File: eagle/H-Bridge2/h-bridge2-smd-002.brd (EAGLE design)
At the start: 100 x 80 mm, 38 parts

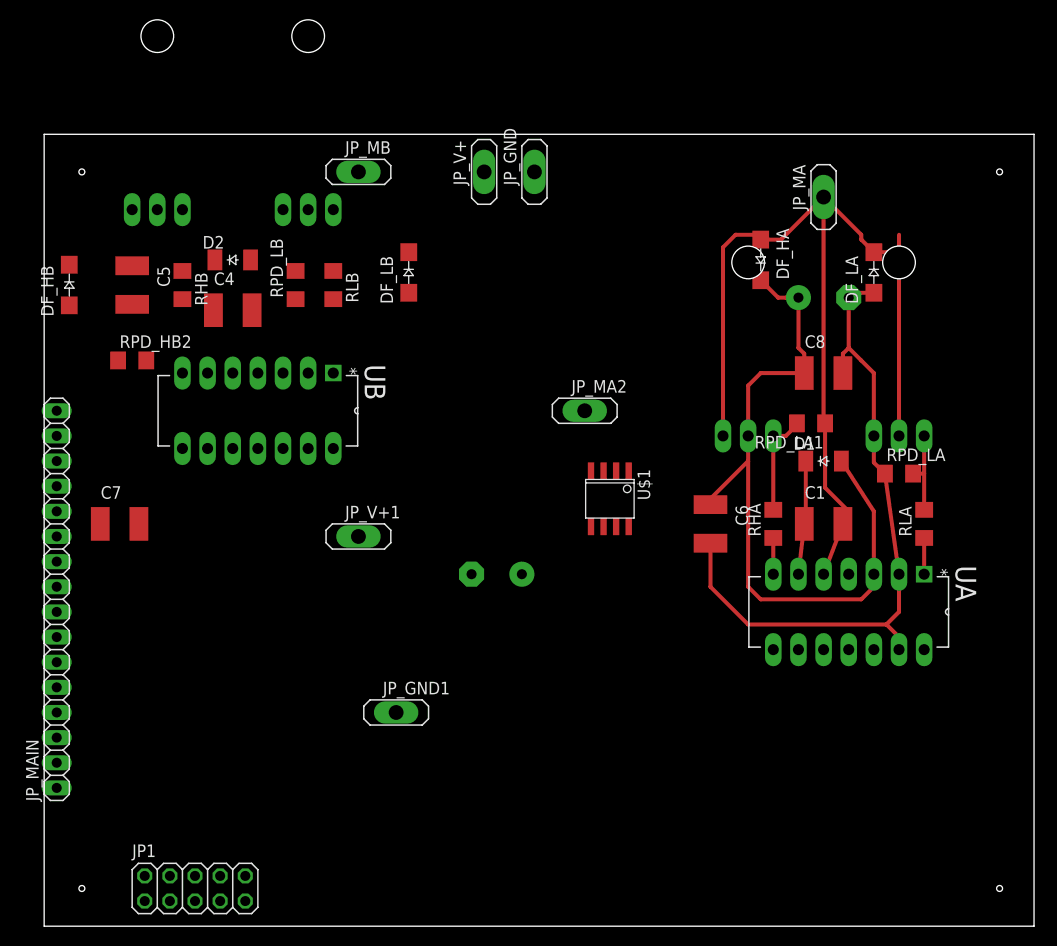
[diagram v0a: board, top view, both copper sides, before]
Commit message: SMD for logic drv
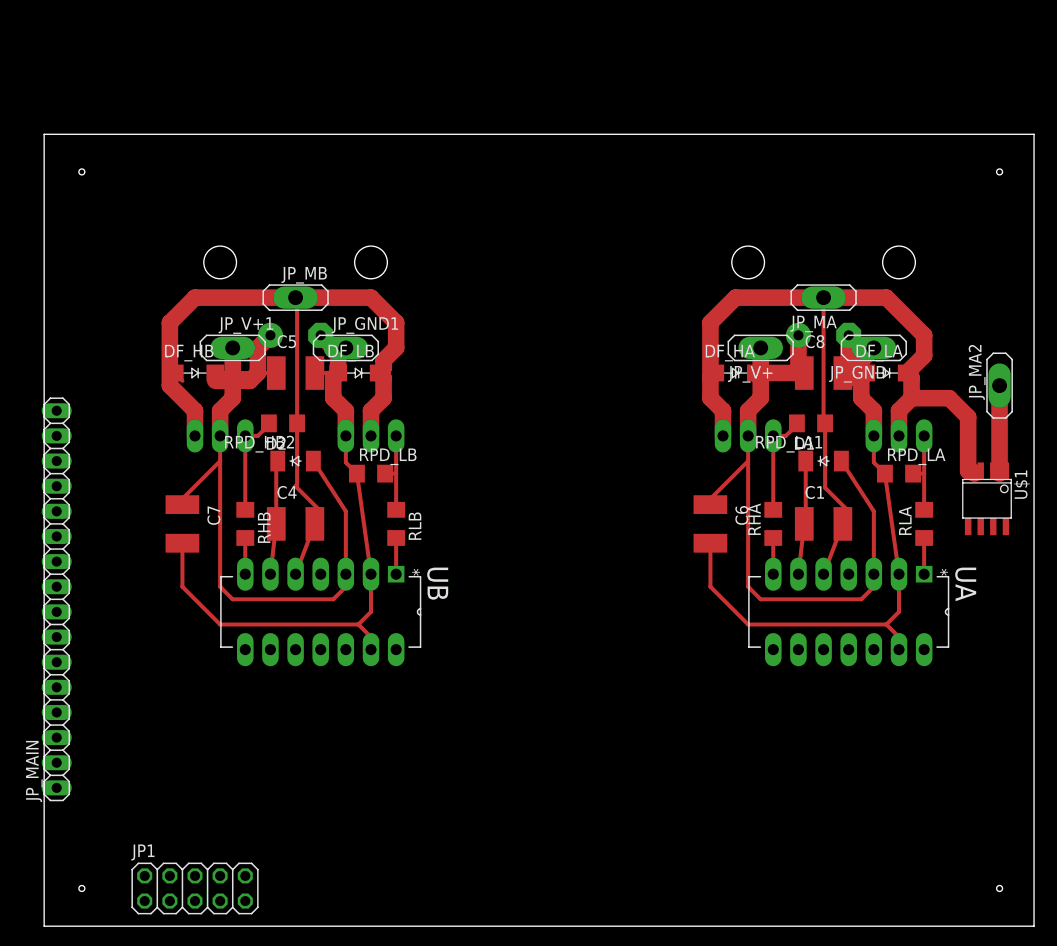
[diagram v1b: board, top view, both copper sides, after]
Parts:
- moved JP_MA2 42.0 mm to (96.5, 54.6), turned to 90 degrees
- moved JP_GND 38.6 mm to (83.8, 58.4), turned to 180 degrees
- moved U$1 38.1 mm to (95.2, 43.2)
- moved JP_GND1 37.2 mm to (30.5, 58.4)
- moved JP_V+ 33.1 mm to (72.4, 58.4), turned to 180 degrees
- moved C9 31.5 mm to (25.4, 59.7), turned to 180 degrees
- moved RHB 25.0 mm to (20.3, 40.6)
- moved RLB 25.0 mm to (35.6, 40.6)
- moved HB 23.7 mm to (17.8, 55.9)
- moved LB 23.7 mm to (33.0, 55.9)
- moved JP_V+1 22.9 mm to (19.1, 58.4)
- moved C4 22.5 mm to (25.4, 40.6)
- moved D2 21.3 mm to (25.4, 47.0)
- moved UB 21.3 mm to (20.3, 27.9)
- moved RPD_LB 20.5 mm to (33.0, 45.7), turned to 0 degrees
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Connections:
- net N$1: now also U$1.1, U$1.2; no longer U$1.3, U$1.4
- net N$17: now also U$1.3, U$1.4; no longer U$1.1, U$1.2
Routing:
- net N$16: track 0.00 -> 81.2 mm
- net N$13: track 74.1 -> 142.0 mm
- net N$4: track 68.4 -> 126.9 mm
- net N$18: track 0.00 -> 11.5 mm
- net N$1: track 0.00 -> 10.9 mm
- net N$17: track 102.2 -> 91.5 mm
- net N$7: track 0.00 -> 10.5 mm
- net N$8: track 0.00 -> 8.59 mm
- net N$12: track 0.00 -> 3.66 mm
- net N$11: track 0.00 -> 3.66 mm

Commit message: SMD for logic drv
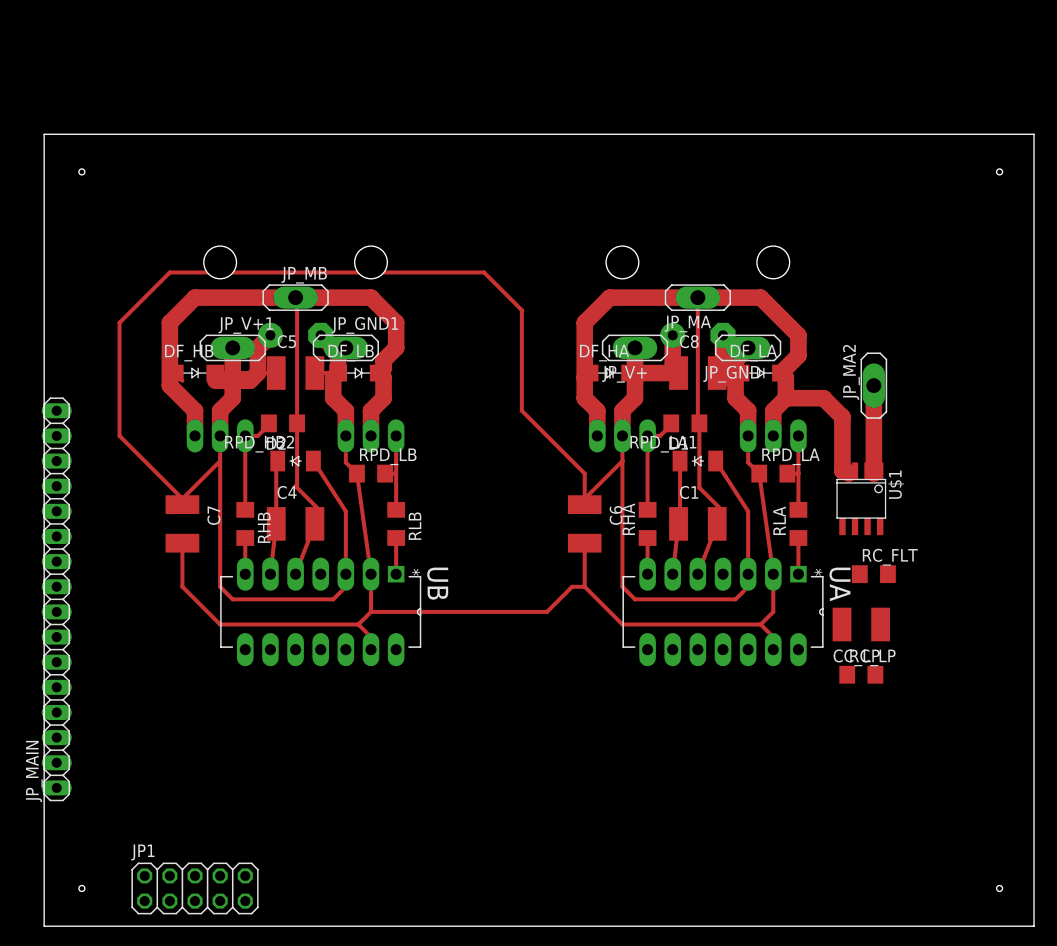
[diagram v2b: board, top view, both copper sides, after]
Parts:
- added CC_LP: (no value), rcl:C4532
- added RC_FLT, RC_LP: (no value), rcl:R1206
- moved C6 12.7 mm to (54.6, 40.6)
- moved DF_LA 12.7 mm to (72.4, 55.9)
- moved HA 12.7 mm to (58.4, 55.9)
- moved JP_MA2 12.7 mm to (83.8, 54.6)
- moved JP_V+ 12.7 mm to (59.7, 58.4)
- moved LA 12.7 mm to (73.7, 55.9)
- moved RLA 12.7 mm to (76.2, 40.6)
- moved RPD_LA 12.7 mm to (73.7, 45.7)
- moved RPD_LA1 12.7 mm to (64.8, 50.8)
- moved U$1 12.7 mm to (82.5, 43.2)
- moved DF_HA 12.7 mm to (57.1, 55.9)
- moved RHA 12.7 mm to (61.0, 40.6)
- moved UA 12.7 mm to (61.0, 27.9)
- moved C1 12.7 mm to (66.0, 40.6)
- moved C3 12.7 mm to (66.0, 59.7)
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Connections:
- new net N$15: CC_LP.1, RC_LP.2, U$1.7
- new net N$19: JP_MAIN.2, RC_LP.1
- new net N$2: JP_MAIN.1, RC_FLT.2, U$1.8
- new net N$21: CC_LP.2, U$1.5
- new net N$3: JP_MAIN.3, RC_FLT.1, U$1.6
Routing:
- net N$13: track 142.0 -> 229.1 mm
- net N$4: track 126.9 -> 149.6 mm

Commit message: Drv signals wiring
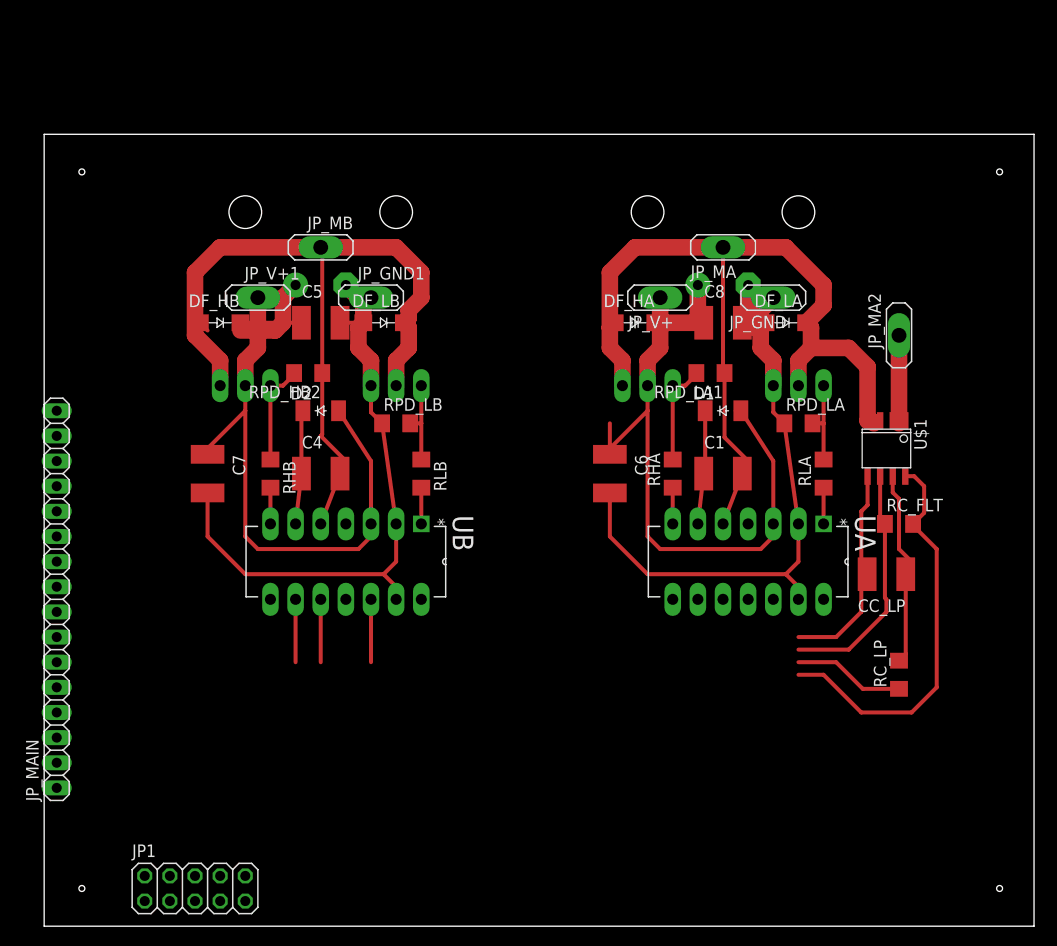
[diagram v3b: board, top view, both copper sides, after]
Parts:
- moved RPD_LA1 5.68 mm to (67.3, 55.9)
- moved RPD_HB2 5.68 mm to (26.7, 55.9)
- moved CC_LP 5.68 mm to (85.1, 35.6)
- moved UA 5.68 mm to (63.5, 33.0)
- moved UB 5.68 mm to (22.9, 33.0)
- moved DF_LA 5.68 mm to (74.9, 61.0)
- moved JP_MA2 5.68 mm to (86.4, 59.7)
- moved LA 5.68 mm to (76.2, 61.0)
- moved RC_FLT 5.68 mm to (86.4, 40.6)
- moved RPD_LA 5.68 mm to (76.2, 50.8)
- moved U$1 5.68 mm to (85.1, 48.3)
- moved C4 5.68 mm to (27.9, 45.7)
- moved C5 5.68 mm to (27.9, 61.0)
- moved C7 5.68 mm to (16.5, 45.7)
- moved C9 5.68 mm to (27.9, 64.8)
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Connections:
- removed net N$27: JP1.6, UB.11
- net N$20: now also UB.11
- net N$21: now also JP_MAIN.4
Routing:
- net N$13: track 229.1 -> 145.2 mm
- net N$2: track 0.00 -> 40.7 mm
- net N$3: track 0.00 -> 24.4 mm
- net N$4: track 149.6 -> 126.9 mm
- net N$21: track 0.00 -> 22.2 mm
- net N$15: track 0.00 -> 20.0 mm
- net N$19: track 0.00 -> 11.3 mm
- net N$28: track 0.00 -> 6.35 mm
- net N$26: track 0.00 -> 6.35 mm
- net N$25: track 0.00 -> 6.35 mm

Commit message: Hbr wiring 0 airways, no polygon
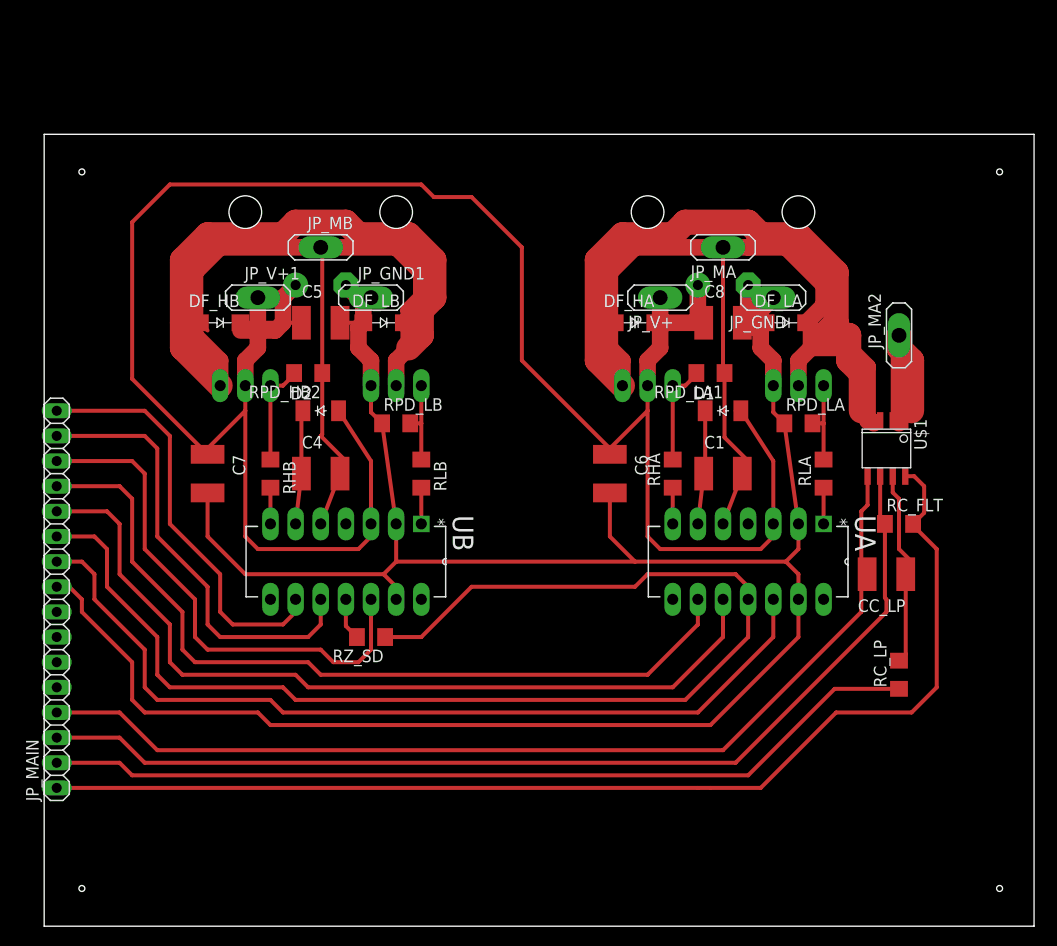
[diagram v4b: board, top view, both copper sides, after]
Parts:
- removed JP1: (no value), pinhead:2X05
- added RZ_SD: (no value), rcl:R1206
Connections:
- new net N$27: JP_MAIN.14, UB.12
- net N$20: now also JP_MAIN.11, RZ_SD.1; no longer JP1.3, UB.11
- net N$22: now also JP_MAIN.13; no longer JP1.7
- net N$23: now also JP_MAIN.12; no longer JP1.5
- net N$24: now also JP_MAIN.10; no longer JP1.1
- net N$25: now also JP_MAIN.16; no longer JP1.2
- net N$26: now also JP_MAIN.15; no longer JP1.4
- net N$28: now also RZ_SD.2, UB.11; no longer JP1.8, UB.12
- net N$4: now also JP_MAIN.9; no longer JP1.9
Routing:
- net N$20: track 0.00 -> 128.7 mm
- net N$4: track 126.9 -> 243.0 mm
- net N$13: track 145.2 -> 236.2 mm
- net N$24: track 0.00 -> 89.4 mm
- net N$23: track 0.00 -> 85.8 mm
- net N$22: track 0.00 -> 83.3 mm
- net N$21: track 22.2 -> 103.5 mm
- net N$3: track 24.4 -> 105.2 mm
- net N$19: track 11.3 -> 89.2 mm
- net N$2: track 40.7 -> 117.2 mm
- net N$17: track 91.5 -> 153.2 mm
- net N$29: track 81.2 -> 137.5 mm
- net N$27: track 0.00 -> 52.5 mm
- net N$26: track 6.35 -> 45.6 mm
- net N$25: track 6.35 -> 42.3 mm
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
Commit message: Hbr wiring 0 airways, with polygon
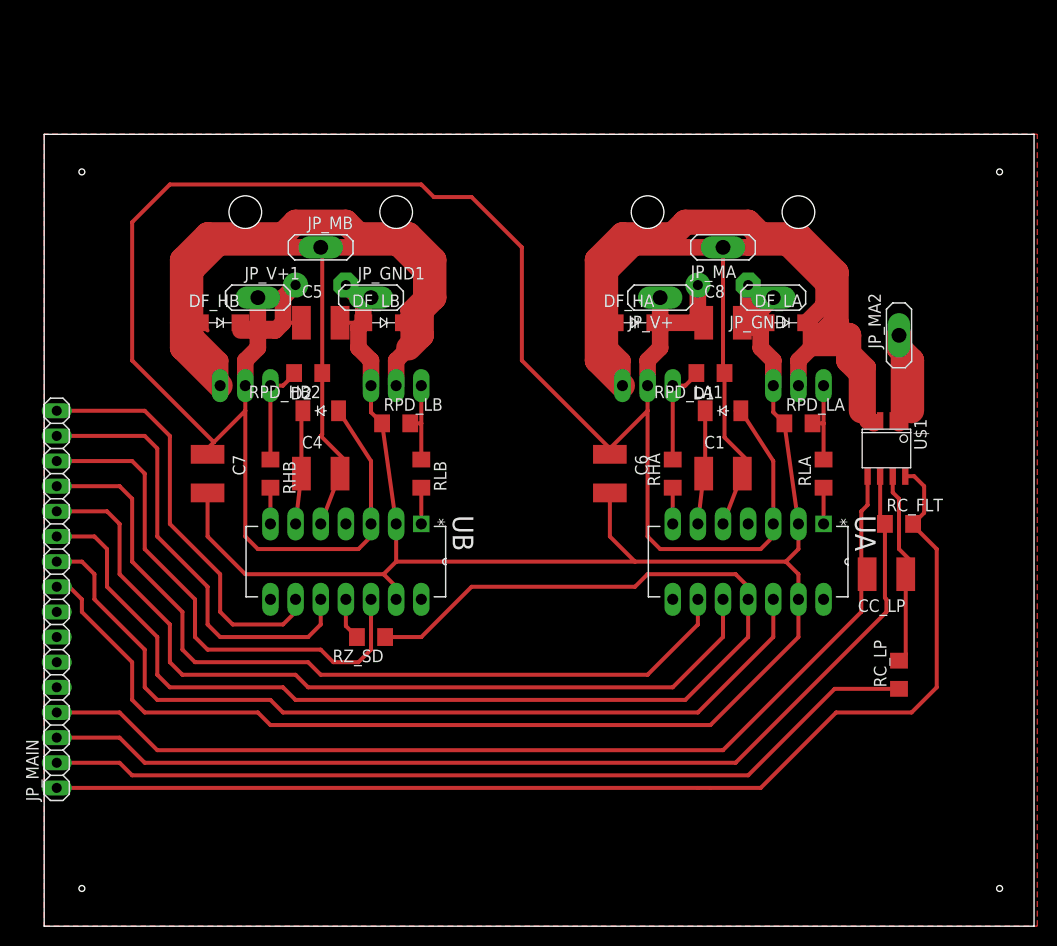
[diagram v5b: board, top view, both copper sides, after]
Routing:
- net N$13: track 236.2 -> 235.3 mm
- added copper zone on layer 1, net N$16
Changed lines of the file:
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@@
 <wire x1="20.32" y1="52.07" x2="20.32" y2="54.61" width="0.4064" layer="1"/>
 <wire x1="16.51" y1="47.67" x2="16.51" y2="48.26" width="0.4064" layer="1"/>
-<wire x1="16.51" y1="48.26" x2="20.32" y2="52.07" width="0.4064" layer="1"/>
+<wire x1="16.51" y1="48.26" x2="17.145" y2="48.895" width="0.4064" layer="1"/>
+<wire x1="17.145" y1="48.895" x2="20.32" y2="52.07" width="0.4064" layer="1"/>
 <wire x1="19.83" y1="60.96" x2="19.83" y2="60.18" width="0.4064" layer="1"/>
 <wire x1="19.83" y1="60.96" x2="24.13" y2="60.96" width="0.4064" layer="1"/>
@@
 <wire x1="38.1" y1="74.93" x2="12.7" y2="74.93" width="0.4064" layer="1"/>
 <wire x1="12.7" y1="74.93" x2="8.89" y2="71.12" width="0.4064" layer="1"/>
-<wire x1="8.89" y1="71.12" x2="8.89" y2="55.29" width="0.4064" layer="1"/>
-<wire x1="8.89" y1="55.29" x2="16.51" y2="47.67" width="0.4064" layer="1"/>
+<wire x1="8.89" y1="71.12" x2="8.89" y2="57.15" width="0.4064" layer="1"/>
+<wire x1="8.89" y1="57.15" x2="17.145" y2="48.895" width="0.4064" layer="1"/>
 </signal>
 <signal name="N$18">
@@
 <wire x1="13.97" y1="60.96" x2="15.73" y2="60.96" width="0.4064" layer="1"/>
 </signal>
+<signal name="N$16">
+<polygon width="0.4064" layer="1" pour="hatch" isolate="1.27">
+<vertex x="0" y="80.01"/>
+<vertex x="0" y="0"/>
+<vertex x="100.33" y="0"/>
+<vertex x="100.33" y="80.01"/>
+</polygon>
+</signal>
 </signals>
